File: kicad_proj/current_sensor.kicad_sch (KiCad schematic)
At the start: 5 parts, among them U1 INA260

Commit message: checked all the schematics
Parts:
- removed U1: INA260, Package_SO:TSSOP-16_4.4x5mm_P0.65mm, symbol Sensor:INA260
- added U1: INA260, rpi_power_warden_hat:TSSOP-16_4.4x5mm_P0.65mm, symbol rpi_power_warden_hat:INA260
- TP2, TP3: now left out of the parts list
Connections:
- net +3V3: now also U1.10 (VS)
- net +VCC_IN: now also U1.1 (IN+), U1.12 (VBUS), U1.2 (IN+), U1.3 (IN+)
- net +VCC_OUT: now also U1.14 (IN-), U1.15 (IN-), U1.16 (IN-)
- net ADDRESS: now also U1.5 (A0)
- net GND: now also U1.11 (GND), U1.4 (A1), U1.6 (GND)
- net INA_SCL: now also U1.9 (SCL)
- net INA_SDA: now also U1.8 (SDA)
- net INA_VCC_ALERT: now also U1.7 (ALERT)
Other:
- moved on the sheet: C1, TP2, TP3

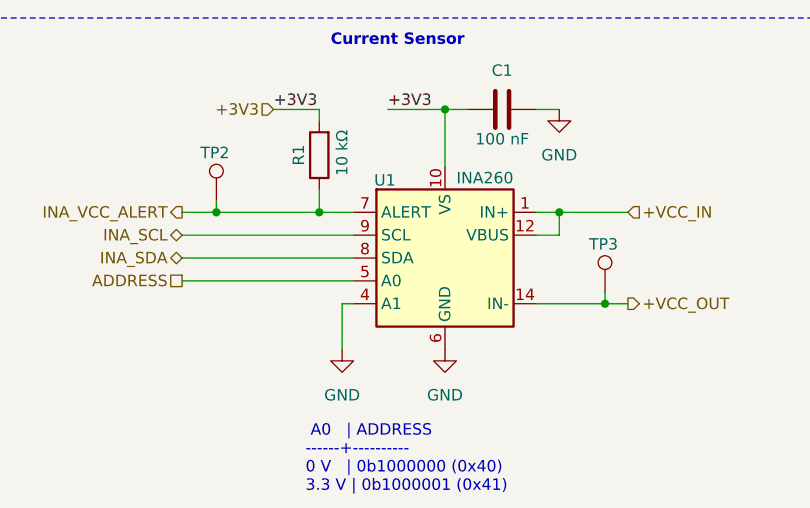
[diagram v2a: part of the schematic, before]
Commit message: finish placement
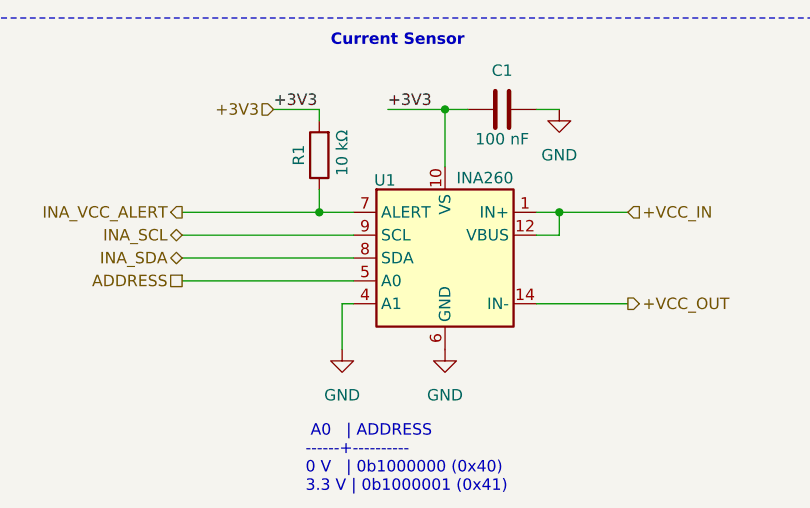
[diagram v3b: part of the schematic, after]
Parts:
- removed TP2, TP3: TestPoint, TestPoint:TestPoint_Pad_D2.5mm, symbol Connector:TestPoint
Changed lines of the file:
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@@
-	)
-	(junction
-		(at 113.03 72.39)
-		(diameter 0)
-		(color 0 0 0 0)
-	)
-	(junction
-		(at 156.21 82.55)
-		(diameter 0)
-		(color 0 0 0 0)
 	)
 	(junction
@@
 	(wire
 		(pts
-			(xy 156.21 81.28) (xy 156.21 82.55)
-		)
-		(stroke
-			(width 0)
-			(type default)
-		)
-	)
-	(wire
-		(pts
 			(xy 148.59 74.93) (xy 151.13 74.93)
 		)
@@
 	(wire
 		(pts
-			(xy 156.21 82.55) (xy 158.75 82.55)
-		)
-		(stroke
-			(width 0)
-			(type default)
-		)
-	)
-	(wire
-		(pts
-			(xy 148.59 82.55) (xy 156.21 82.55)
+			(xy 148.59 82.55) (xy 158.75 82.55)
 		)
 		(stroke
@@
 	(wire
 		(pts
-			(xy 113.03 72.39) (xy 124.46 72.39)
-		)
-		(stroke
-			(width 0)
-			(type default)
-		)
-	)
-	(wire
-		(pts
 			(xy 148.59 72.39) (xy 151.13 72.39)
 		)
@@
 	(wire
 		(pts
-			(xy 113.03 71.12) (xy 113.03 72.39)
-		)
-		(stroke
-			(width 0)
-			(type default)
-		)
-	)
-	(wire
-		(pts
-			(xy 109.22 72.39) (xy 113.03 72.39)
+			(xy 109.22 72.39) (xy 124.46 72.39)
 		)
 		(stroke
@@
 					(unit 1)
 				)
-			)
-		)
-	)
-	(symbol
-		(lib_id "Connector:TestPoint")
-		(at 113.03 71.12 0)
-		(unit 1)
-		(exclude_from_sim no)
-		(in_bom no)
-		(on_board yes)
-		(dnp no)
-		(property "Reference" "TP2"
-			(at 111.252 65.786 0)
-			(effects
-				(font
-					(size 1.27 1.27)
-				)
-				(justify left)
-			)
-		)
-		(property "Value" "TestPoint"
-			(at 115.57 69.0879 0)
-			(effects
-				(font
-					(size 1.27 1.27)
-				)
-				(justify left)
-				(hide yes)
-			)
-		)
-		(property "Footprint" "TestPoint:TestPoint_Pad_D2.5mm"
-			(at 118.11 71.12 0)
-			(effects
-				(font
-					(size 1.27 1.27)
-				)
-				(hide yes)
-			)
-		)
-		(property "Datasheet" "~"
-			(at 118.11 71.12 0)
-			(effects
-				(font
-					(size 1.27 1.27)
-				)
-				(hide yes)
-			)
-		)
-		(property "Description" "test point"
-			(at 113.03 71.12 0)
-			(effects
-				(font
-					(size 1.27 1.27)
-				)
-				(hide yes)
-			)
-		)
-		(pin "1"
-		)
-		(instances
-			(project "rpi_power_warden_hat"
-				(path "/8692c5de-a943-41e8-8e29-f6c5e99cda34/280f8587-5166-4f13-bc2f-0b642f6ac80b"
-					(reference "TP2")
-					(unit 1)
-				)
-				(path "/8692c5de-a943-41e8-8e29-f6c5e99cda34/52241f92-cbdb-484e-bc49-950aa69fc821"
-					(reference "TP4")
-					(unit 1)
-				)
-			)
-		)
-	)
-	(symbol
-		(lib_id "Connector:TestPoint")
-		(at 156.21 81.28 0)
-		(unit 1)
-		(exclude_from_sim no)
-		(in_bom no)
-		(on_board yes)
-		(dnp no)
-		(property "Reference" "TP3"
-			(at 154.432 75.946 0)
-			(effects
-				(font
-					(size 1.27 1.27)
-				)
-				(justify left)
-			)
-		)
-		(property "Value" "TestPoint"
-			(at 158.75 79.2479 0)
-			(effects
-				(font
-					(size 1.27 1.27)
-				)
-				(justify left)
-				(hide yes)
-			)
-		)
-		(property "Footprint" "TestPoint:TestPoint_Pad_D2.5mm"
-			(at 161.29 81.28 0)
-			(effects
-				(font
-					(size 1.27 1.27)
-				)
-				(hide yes)
-			)
-		)
-		(property "Datasheet" "~"
-			(at 161.29 81.28 0)
-			(effects
-				(font
-					(size 1.27 1.27)
-				)
-				(hide yes)
-			)
-		)
-		(property "Description" "test point"
-			(at 156.21 81.28 0)
-			(effects
-				(font
-					(size 1.27 1.27)
-				)
-				(hide yes)
-			)
-		)
-		(pin "1"
-		)
-		(instances
-			(project "rpi_power_warden_hat"
-				(path "/8692c5de-a943-41e8-8e29-f6c5e99cda34/280f8587-5166-4f13-bc2f-0b642f6ac80b"
-					(reference "TP3")
-					(unit 1)
-				)
-				(path "/8692c5de-a943-41e8-8e29-f6c5e99cda34/52241f92-cbdb-484e-bc49-950aa69fc821"
-					(reference "TP5")
-					(unit 1)
-				)
